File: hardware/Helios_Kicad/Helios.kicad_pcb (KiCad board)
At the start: 2 copper layers, 75.2 x 61.1 mm, 101 parts, among them P1 USB_B, P2 CONN_01X25-SHIELD, U1 IP4220CZ6, U2 AP2114, U3 AN431B, U4 ISA_DC-DC_converter, U5 DAC084S085C, U6 TL084_v, U7 LM358, U8 TL084_v, U9 ATSAM4S, Y1 16MHz 18pF

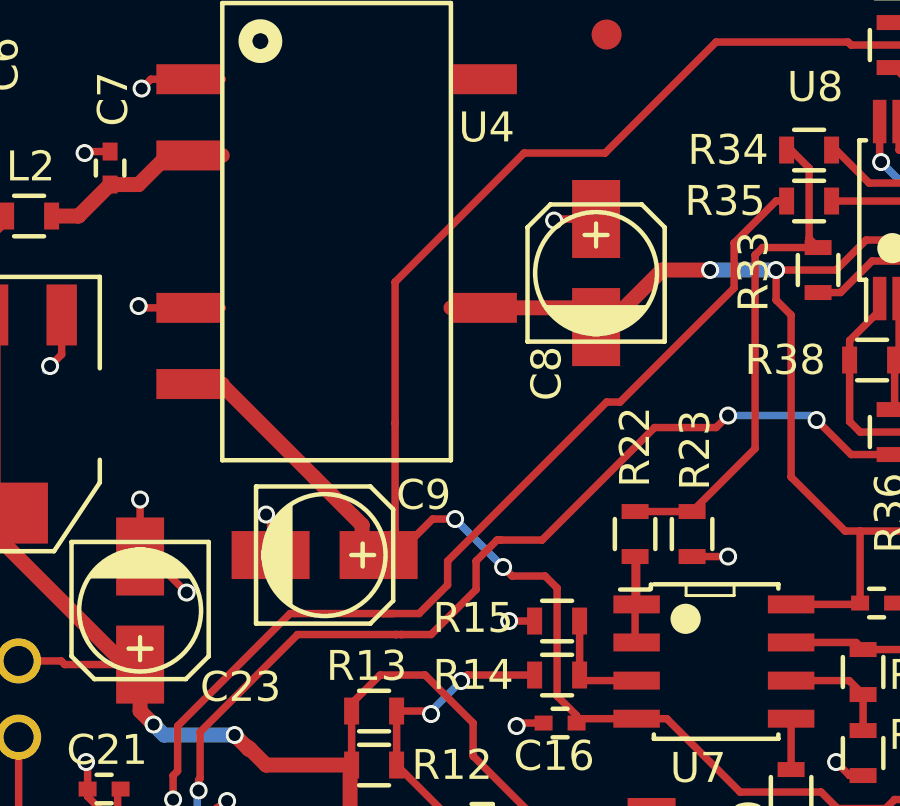
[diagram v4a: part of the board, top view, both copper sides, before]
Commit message: capacitors wrong polarity
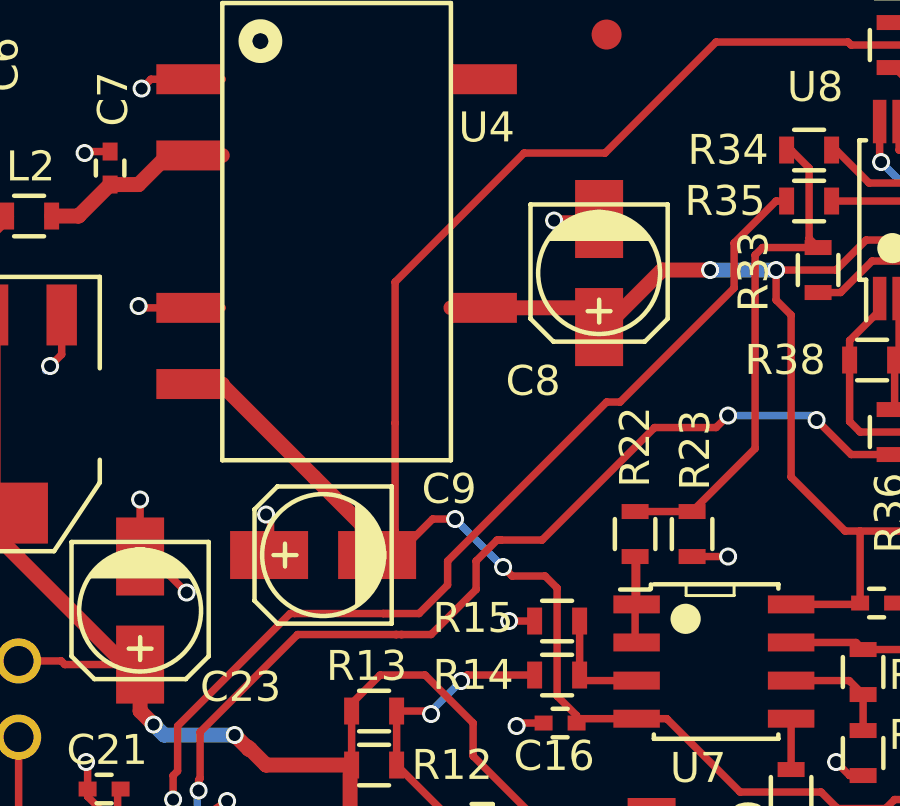
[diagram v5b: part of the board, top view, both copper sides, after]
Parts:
- moved C8 0.10 mm to (142.0, 114.0), turned to 270 degrees
- turned C9 to 180 degrees
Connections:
- C8 pad 1: GND -> /Amplifiers/+9V
- C8 pad 2: /Amplifiers/+9V -> GND
- C9 pad 1: /Amplifiers/-9V -> GND
- C9 pad 2: GND -> /Amplifiers/-9V
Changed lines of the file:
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@@
   )
   (module Capacitors_SMD:c_elec_4x5.3 (layer F.Cu)
-    (at 141.9 114 90)
+    (at 142 114 270)
     (descr "SMT capacitor, aluminium electrolytic, 4x5.3")
     (attr smd)
-    (fp_text reference C8 (at -3.35 -1.65 90) (layer F.SilkS)
-      (effects (font (size 1 1) (thickness 0.15)))
-    )
-    (fp_text value 4.7uF (at 0 3.175 90) (layer F.Fab)
+    (fp_text reference C8 (at 3.6 2.2 360) (layer F.SilkS)
+      (effects (font (size 1 1) (thickness 0.15)))
+    )
+    (fp_text value 4.7uF (at 0 3.175 270) (layer F.Fab)
       (effects (font (size 1 1) (thickness 0.15)))
     )
@@
     (fp_line (start -2.286 -2.286) (end -2.286 2.286) (layer F.SilkS) (width 0.15))
     (fp_circle (center 0 0) (end -2.032 0) (layer F.SilkS) (width 0.15))
-    (pad 1 smd rect (at 1.80086 0 90) (size 2.60096 1.6002) (layers F.Cu F.Paste F.Mask)
+    (pad 1 smd rect (at 1.80086 0 270) (size 2.60096 1.6002) (layers F.Cu F.Paste F.Mask)
+      (net 7 /Amplifiers/+9V))
+    (pad 2 smd rect (at -1.80086 0 270) (size 2.60096 1.6002) (layers F.Cu F.Paste F.Mask)
       (net 2 GND))
-    (pad 2 smd rect (at -1.80086 0 90) (size 2.60096 1.6002) (layers F.Cu F.Paste F.Mask)
-      (net 7 /Amplifiers/+9V))
     (model Capacitors_SMD.3dshapes/c_elec_4x5.3.wrl
       (at (xyz 0 0 0))
@@
   )
   (module Capacitors_SMD:c_elec_4x5.3 (layer F.Cu)
-    (at 132.85 123.4)
+    (at 132.8 123.4 180)
     (descr "SMT capacitor, aluminium electrolytic, 4x5.3")
     (attr smd)
-    (fp_text reference C9 (at 3.3 -2) (layer F.SilkS)
-      (effects (font (size 1 1) (thickness 0.15)))
-    )
-    (fp_text value 4.7uF (at 0 3.175) (layer F.Fab)
+    (fp_text reference C9 (at -4.2 2.2 180) (layer F.SilkS)
+      (effects (font (size 1 1) (thickness 0.15)))
+    )
+    (fp_text value 4.7uF (at 0 3.175 180) (layer F.Fab)
       (effects (font (size 1 1) (thickness 0.15)))
     )
@@
     (fp_line (start -2.286 -2.286) (end -2.286 2.286) (layer F.SilkS) (width 0.15))
     (fp_circle (center 0 0) (end -2.032 0) (layer F.SilkS) (width 0.15))
-    (pad 1 smd rect (at 1.80086 0) (size 2.60096 1.6002) (layers F.Cu F.Paste F.Mask)
+    (pad 1 smd rect (at 1.80086 0 180) (size 2.60096 1.6002) (layers F.Cu F.Paste F.Mask)
+      (net 2 GND))
+    (pad 2 smd rect (at -1.80086 0 180) (size 2.60096 1.6002) (layers F.Cu F.Paste F.Mask)
       (net 8 /Amplifiers/-9V))
-    (pad 2 smd rect (at -1.80086 0) (size 2.60096 1.6002) (layers F.Cu F.Paste F.Mask)
-      (net 2 GND))
     (model Capacitors_SMD.3dshapes/c_elec_4x5.3.wrl
       (at (xyz 0 0 0))
@@
   (segment (start 126.7 123.44914) (end 126.7 121.55) (width 0.25) (layer F.Cu) (net 2))
   (via (at 126.7 121.55) (size 0.6) (drill 0.4) (layers F.Cu B.Cu) (net 2))
-  (segment (start 131.04914 123.4) (end 131.04914 122.19914) (width 0.25) (layer F.Cu) (net 2))
-  (via (at 130.9 122.05) (size 0.6) (drill 0.4) (layers F.Cu B.Cu) (net 2))
-  (segment (start 131.04914 122.19914) (end 130.9 122.05) (width 0.25) (layer F.Cu) (net 2))
-  (segment (start 141.9 112.19914) (end 140.55086 112.19914) (width 0.25) (layer F.Cu) (net 2))
-  (via (at 140.5 112.25) (size 0.6) (drill 0.4) (layers F.Cu B.Cu) (net 2))
-  (segment (start 140.55086 112.19914) (end 140.5 112.25) (width 0.25) (layer F.Cu) (net 2))
   (segment (start 132.45 153.05086) (end 131.05086 153.05086) (width 0.25) (layer F.Cu) (net 2))
   (via (at 131 153) (size 0.6) (drill 0.4) (layers F.Cu B.Cu) (net 2))
@@
   (segment (start 124.95 145) (end 125.35 145.4) (width 0.25) (layer F.Cu) (net 2))
   (segment (start 125.35 145.8) (end 125.95 145.8) (width 0.25) (layer F.Cu) (net 2))
+  (segment (start 131.04914 123.4) (end 131.04914 122.19914) (width 0.25) (layer F.Cu) (net 2))
+  (via (at 130.9 122.05) (size 0.6) (drill 0.4) (layers F.Cu B.Cu) (net 2))
+  (segment (start 131.04914 122.19914) (end 130.9 122.05) (width 0.25) (layer F.Cu) (net 2))
+  (segment (start 141.9 112.19914) (end 140.55086 112.19914) (width 0.25) (layer F.Cu) (net 2))
+  (via (at 140.5 112.25) (size 0.6) (drill 0.4) (layers F.Cu B.Cu) (net 2))
+  (segment (start 140.55086 112.19914) (end 140.5 112.25) (width 0.25) (layer F.Cu) (net 2))
   (segment (start 109.051 124.98052) (end 109.051 123.801) (width 0.5) (layer F.Cu) (net 3))
   (segment (start 109.051 123.801) (end 107.4 122.15) (width 0.5) (layer F.Cu) (net 3))
@@
   (segment (start 123.75 112.1) (end 124.65 112.1) (width 0.5) (layer F.Cu) (net 6))
   (segment (start 124.65 112.1) (end 125.7 111.05) (width 0.5) (layer F.Cu) (net 6))
-  (segment (start 137.06 115.16) (end 141.25914 115.16) (width 0.5) (layer F.Cu) (net 7))
   (segment (start 141.25914 115.16) (end 141.9 115.80086) (width 0.25) (layer F.Cu) (net 7))
   (segment (start 141.9 115.80086) (end 142.19914 115.80086) (width 0.25) (layer F.Cu) (net 7))
@@
   (segment (start 159.55 127.25) (end 156.9 124.6) (width 0.25) (layer B.Cu) (net 7))
   (via (at 159.55 127.25) (size 0.6) (drill 0.4) (layers F.Cu B.Cu) (net 7))
+  (segment (start 137.06 115.16) (end 141.25914 115.16) (width 0.5) (layer F.Cu) (net 7))
   (segment (start 155.45 140.5) (end 156 139.95) (width 0.25) (layer F.Cu) (net 7))
   (via (at 155.45 140.5) (size 0.6) (drill 0.4) (layers F.Cu B.Cu) (net 7))
@@
   (segment (start 135.25 123.4) (end 136.45 122.2) (width 0.25) (layer F.Cu) (net 8))
   (segment (start 136.45 122.2) (end 137.2 122.2) (width 0.25) (layer F.Cu) (net 8))
-  (segment (start 132.5 120.8) (end 134.1 122.4) (width 0.5) (layer F.Cu) (net 8))
-  (segment (start 129.44 117.74) (end 132.5 120.8) (width 0.5) (layer F.Cu) (net 8))
   (segment (start 134.1 122.4) (end 134.1 122.84914) (width 0.5) (layer F.Cu) (net 8))
   (segment (start 134.1 122.84914) (end 134.65086 123.4) (width 0.5) (layer F.Cu) (net 8))
-  (segment (start 140.6 128.1) (end 141.25 128.75) (width 0.25) (layer F.Cu) (net 8))
-  (segment (start 140.6 124.5) (end 140.6 128.1) (width 0.25) (layer F.Cu) (net 8))
-  (segment (start 140.2 124.1) (end 140.6 124.5) (width 0.25) (layer F.Cu) (net 8))
-  (segment (start 139.1 124.1) (end 140.2 124.1) (width 0.25) (layer F.Cu) (net 8))
-  (segment (start 138.8 123.8) (end 139.1 124.1) (width 0.25) (layer F.Cu) (net 8))
-  (via (at 138.8 123.8) (size 0.6) (drill 0.4) (layers F.Cu B.Cu) (net 8))
-  (segment (start 137.2 122.2) (end 138.8 123.8) (width 0.25) (layer B.Cu) (net 8))
   (via (at 137.2 122.2) (size 0.6) (drill 0.4) (layers F.Cu B.Cu) (net 8))
   (segment (start 134.4 123.4) (end 135.2 122.6) (width 0.25) (layer F.Cu) (net 8))
@@
   (segment (start 145.9 106.3) (end 150.3 106.3) (width 0.25) (layer F.Cu) (net 8))
   (segment (start 150.3 106.3) (end 150.4 106.4) (width 0.25) (layer F.Cu) (net 8))
+  (segment (start 132.5 120.8) (end 134.1 122.4) (width 0.5) (layer F.Cu) (net 8))
+  (segment (start 137.2 122.2) (end 138.8 123.8) (width 0.25) (layer B.Cu) (net 8))
+  (segment (start 129.44 117.74) (end 132.5 120.8) (width 0.5) (layer F.Cu) (net 8))
+  (segment (start 140.6 128.1) (end 141.25 128.75) (width 0.25) (layer F.Cu) (net 8))
+  (segment (start 140.6 124.5) (end 140.6 128.1) (width 0.25) (layer F.Cu) (net 8))
+  (segment (start 140.2 124.1) (end 140.6 124.5) (width 0.25) (layer F.Cu) (net 8))
+  (segment (start 139.1 124.1) (end 140.2 124.1) (width 0.25) (layer F.Cu) (net 8))
+  (segment (start 138.8 123.8) (end 139.1 124.1) (width 0.25) (layer F.Cu) (net 8))
+  (via (at 138.8 123.8) (size 0.6) (drill 0.4) (layers F.Cu B.Cu) (net 8))
   (segment (start 155.05 135) (end 154.8 135) (width 0.25) (layer F.Cu) (net 8))
   (segment (start 154.8 135) (end 154.05 134.25) (width 0.25) (layer F.Cu) (net 8))

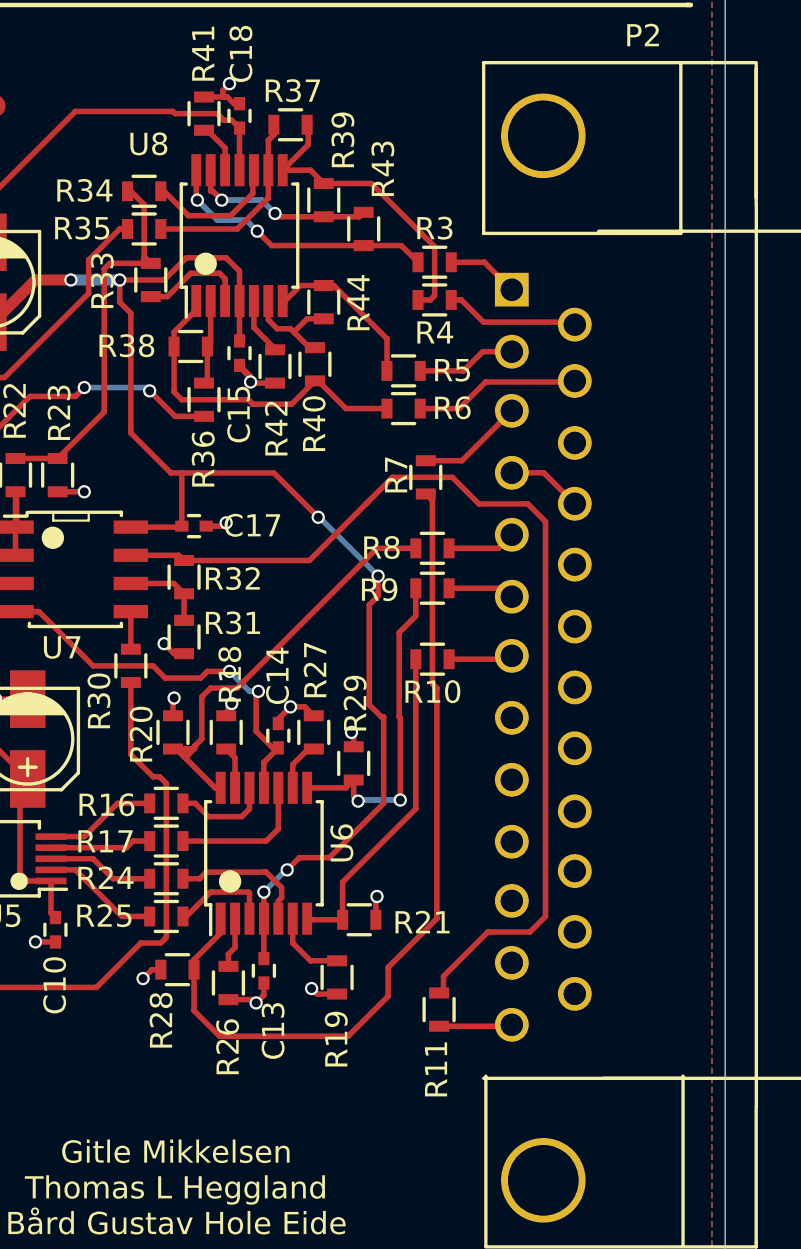
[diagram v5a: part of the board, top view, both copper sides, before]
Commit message: fix color amps error
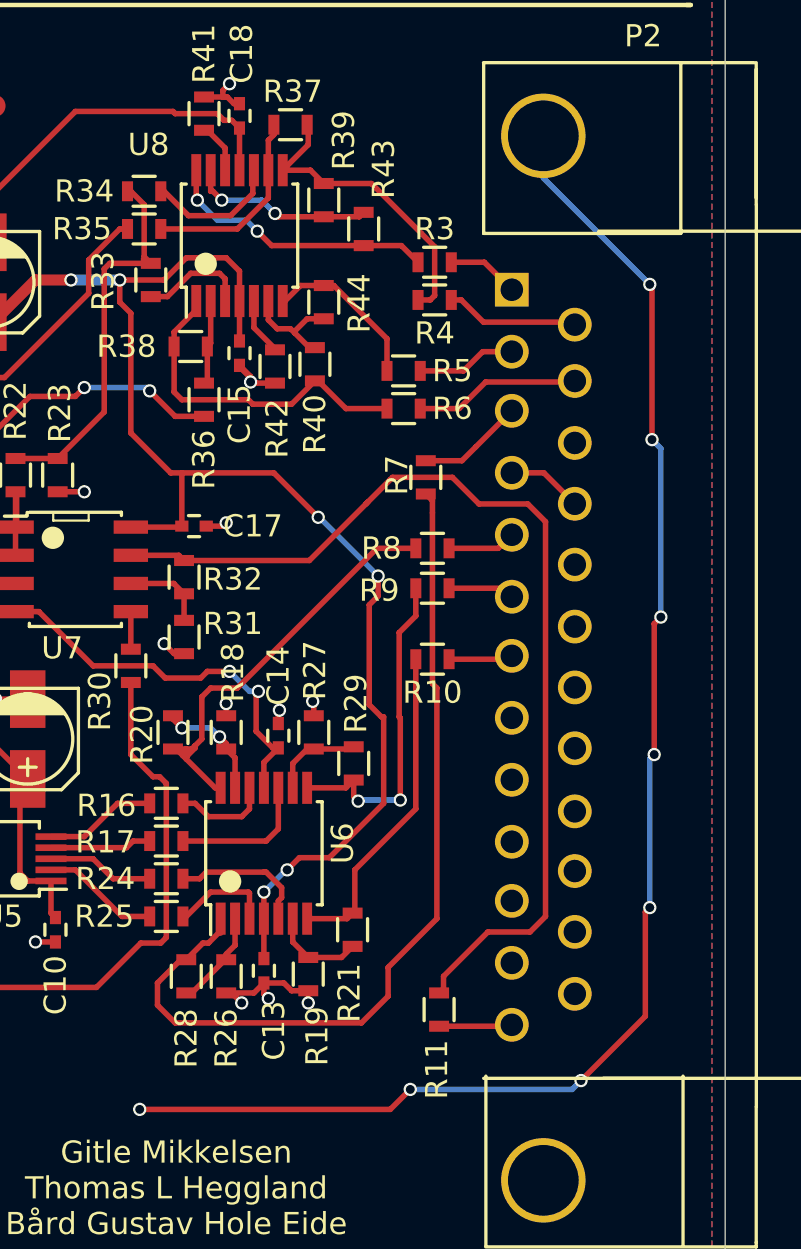
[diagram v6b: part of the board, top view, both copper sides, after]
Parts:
- moved R19 1.31 mm to (156.4, 145.2), turned to 270 degrees
- moved R21 0.54 mm to (158.4, 143.2), turned to 270 degrees
- moved R28 0.50 mm to (150.9, 145.3), turned to 270 degrees
- moved R26 0.32 mm to (152.7, 145.3), turned to 270 degrees
- turned R18 to 90 degrees
- turned R27 to 90 degrees
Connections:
- R18 pad 1: GND -> Net-(R18-Pad1)
- R18 pad 2: Net-(R18-Pad2) -> GND
- R19 pad 1: GND -> Net-(R19-Pad1)
- R19 pad 2: Net-(R19-Pad2) -> GND
- R20 pad 2: GND -> Net-(R18-Pad1)
- R21 pad 2: GND -> Net-(R19-Pad1)
- R26 pad 1: GND -> Net-(R26-Pad1)
- R26 pad 2: Net-(R26-Pad2) -> GND
- R27 pad 1: GND -> Net-(R27-Pad1)
- R27 pad 2: Net-(R27-Pad2) -> GND
- R28 pad 2: GND -> Net-(R26-Pad1)
- R29 pad 2: GND -> Net-(R27-Pad1)
- U6 pad 13: Net-(R18-Pad2) -> Net-(R18-Pad1)
- U6 pad 2: Net-(R26-Pad2) -> Net-(R26-Pad1)
- U6 pad 6: Net-(R19-Pad2) -> Net-(R19-Pad1)
- U6 pad 9: Net-(R27-Pad2) -> Net-(R27-Pad1)
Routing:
- net GND: track 73.7 -> 138.7 mm, vias 49 -> 55
- net Net-(R18-Pad1): track 0.00 -> 5.17 mm, vias 0 -> 2
- net Net-(R26-Pad1): track 0.00 -> 4.44 mm
- net Net-(R27-Pad1): track 0.00 -> 4.41 mm
- net Net-(R19-Pad1): track 0.00 -> 4.25 mm
- net Net-(R19-Pad2): track 3.43 -> 0.00 mm
- net /Amplifiers/+Intensity: track 38.9 -> 41.5 mm
- net Net-(R27-Pad2): track 2.29 -> 0.00 mm
- net Net-(R26-Pad2): track 2.27 -> 0.00 mm
- net Net-(R18-Pad2): track 1.92 -> 0.00 mm

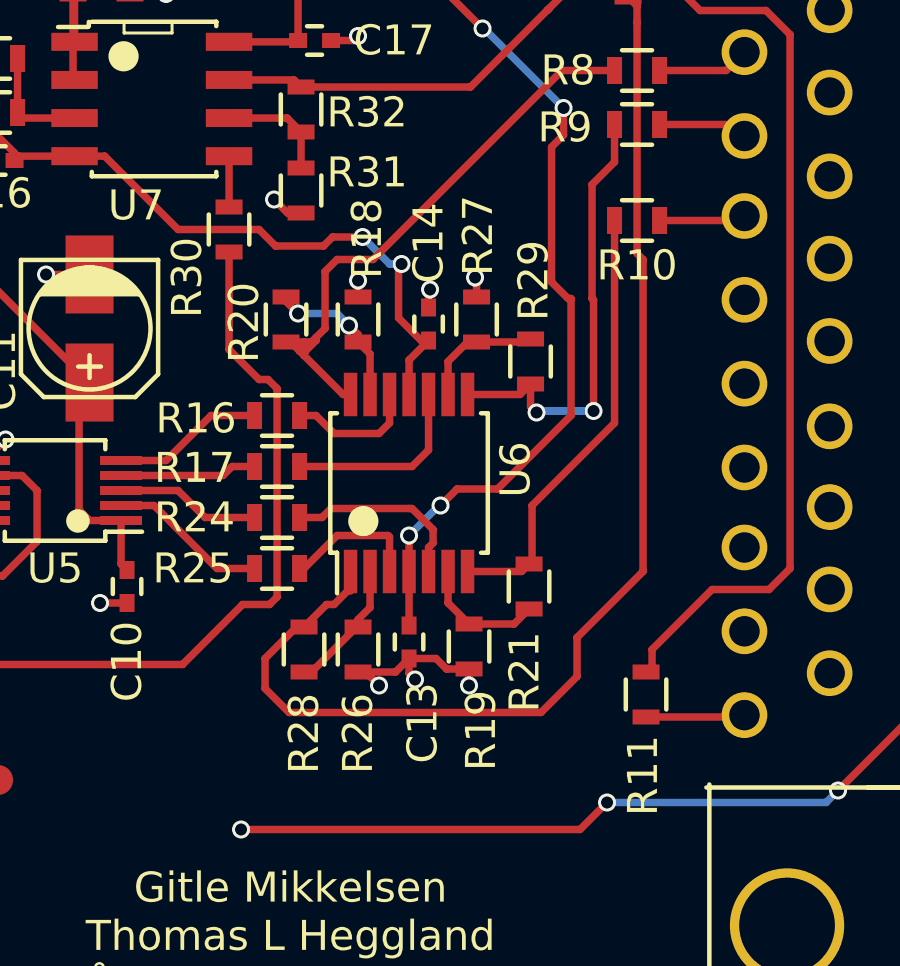
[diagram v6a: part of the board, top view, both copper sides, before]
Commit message: removed uneccessary resistors
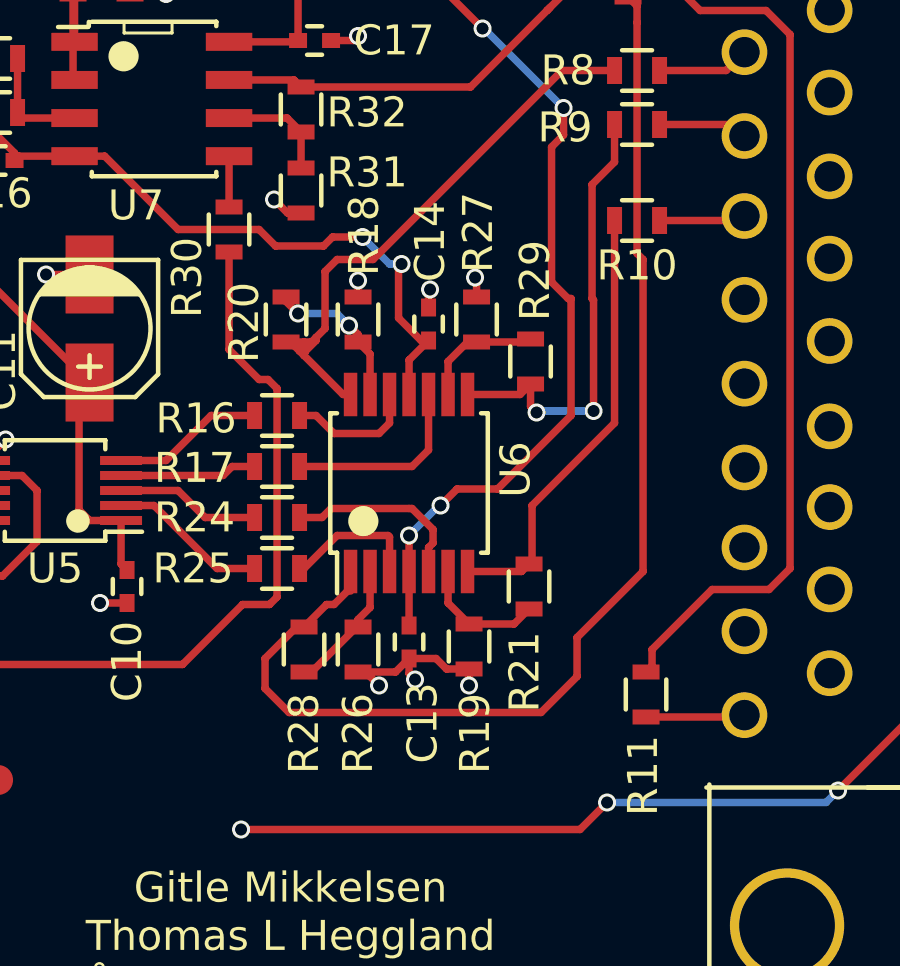
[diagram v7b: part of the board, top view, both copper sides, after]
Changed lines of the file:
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@@
     (tags "capacitor 0402")
     (attr smd)
-    (fp_text reference C14 (at -2.7 0 270) (layer F.SilkS)
+    (fp_text reference C14 (at -2.75 -0.05 270) (layer F.SilkS)
       (effects (font (size 1 1) (thickness 0.15)))
     )
@@
     (tags "resistor 0603")
     (attr smd)
-    (fp_text reference R18 (at 2.7 0.3 90) (layer F.SilkS)
+    (fp_text reference R18 (at 2.8 0.2 90) (layer F.SilkS)
       (effects (font (size 1 1) (thickness 0.15)))
     )
@@
     (tags "resistor 0603")
     (attr smd)
-    (fp_text reference R19 (at 2.8 -0.4 270) (layer F.SilkS)
+    (fp_text reference R19 (at 2.9 -0.2 270) (layer F.SilkS)
       (effects (font (size 1 1) (thickness 0.15)))
     )
@@
     (tags "resistor 0603")
     (attr smd)
-    (fp_text reference R27 (at 2.8 0.05 90) (layer F.SilkS)
+    (fp_text reference R27 (at 2.9 0.05 90) (layer F.SilkS)
       (effects (font (size 1 1) (thickness 0.15)))
     )
@@
     (tags "resistor 0603")
     (attr smd)
-    (fp_text reference R29 (at 2.7 0.1 90) (layer F.SilkS)
+    (fp_text reference R29 (at 2.7 0.15 90) (layer F.SilkS)
       (effects (font (size 1 1) (thickness 0.15)))
     )
@@
   (segment (start 109.80086 116.1) (end 109.20086 115.5) (width 0.5) (layer F.Cu) (net 1))
   (segment (start 112.1 118.85) (end 112.1 116.1) (width 0.5) (layer F.Cu) (net 1))
-  (segment (start 167 107.4) (end 167 109.3) (width 0.25) (layer B.Cu) (net 2) (status C00000))
-  (segment (start 167 109.3) (end 171.8 114.1) (width 0.25) (layer B.Cu) (net 2) (status 400000))
+  (segment (start 167 107.4) (end 167 109.3) (width 0.25) (layer B.Cu) (net 2))
+  (segment (start 167 109.3) (end 171.8 114.1) (width 0.25) (layer B.Cu) (net 2))
   (via (at 171.8 114.1) (size 0.6) (drill 0.4) (layers F.Cu B.Cu) (net 2))
   (segment (start 171.8 114.1) (end 171.9 114.2) (width 0.25) (layer F.Cu) (net 2))
